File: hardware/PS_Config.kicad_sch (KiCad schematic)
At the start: 22 parts, among them J3 Micro_SD_Card, SW2 SW_DIP_x01, U13 TXS0206A, U2 xc7z020clg400, X2 SiT1602B

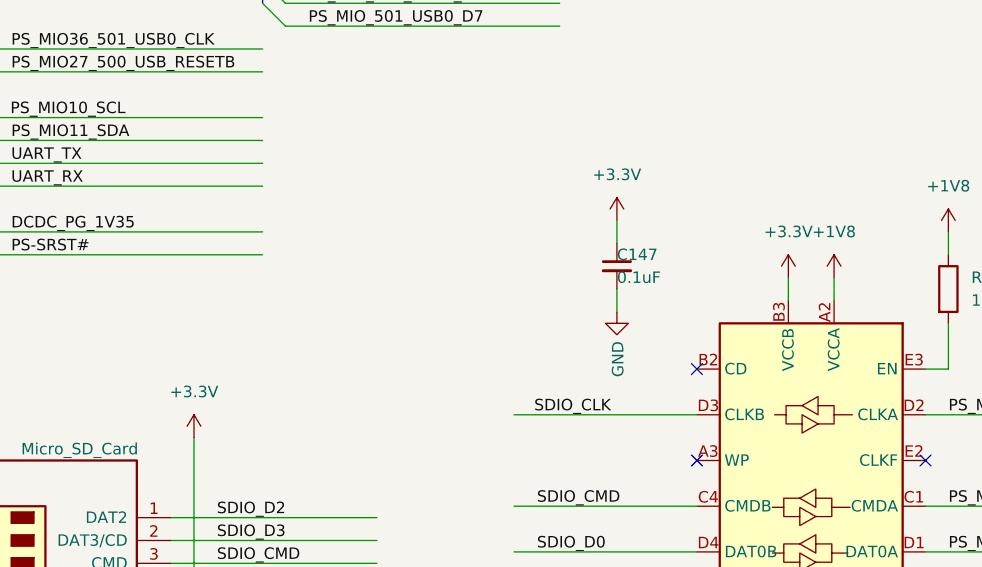
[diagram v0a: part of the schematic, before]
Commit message: delete RF transceiver
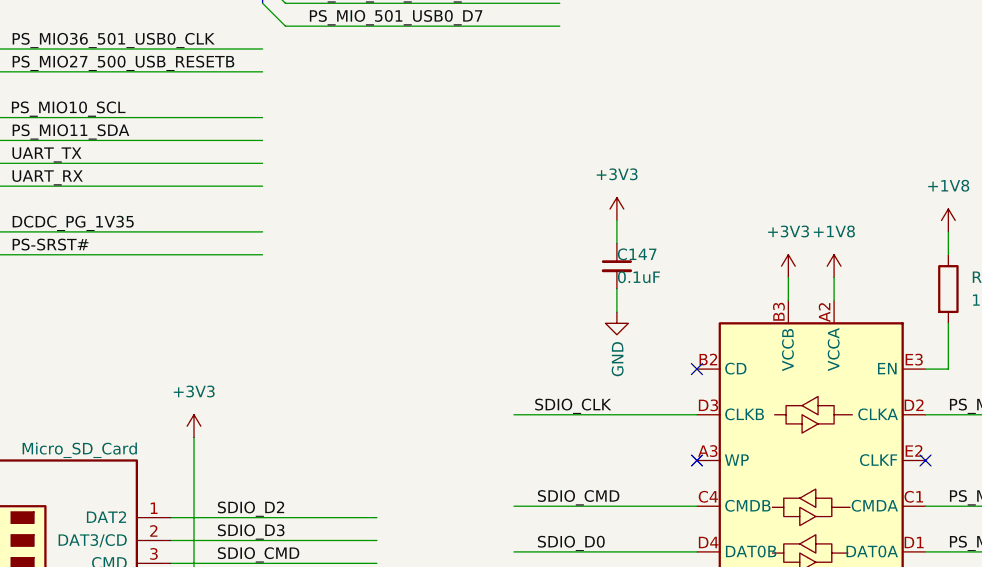
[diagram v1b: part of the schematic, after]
